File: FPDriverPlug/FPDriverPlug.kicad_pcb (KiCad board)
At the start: 2 copper layers, 21 x 61.6 mm, 4 parts, among them CN1 Conn_02x05_Odd_Even, CN2 Conn_02x16_Counter_Clockwise, U1 FP2800A

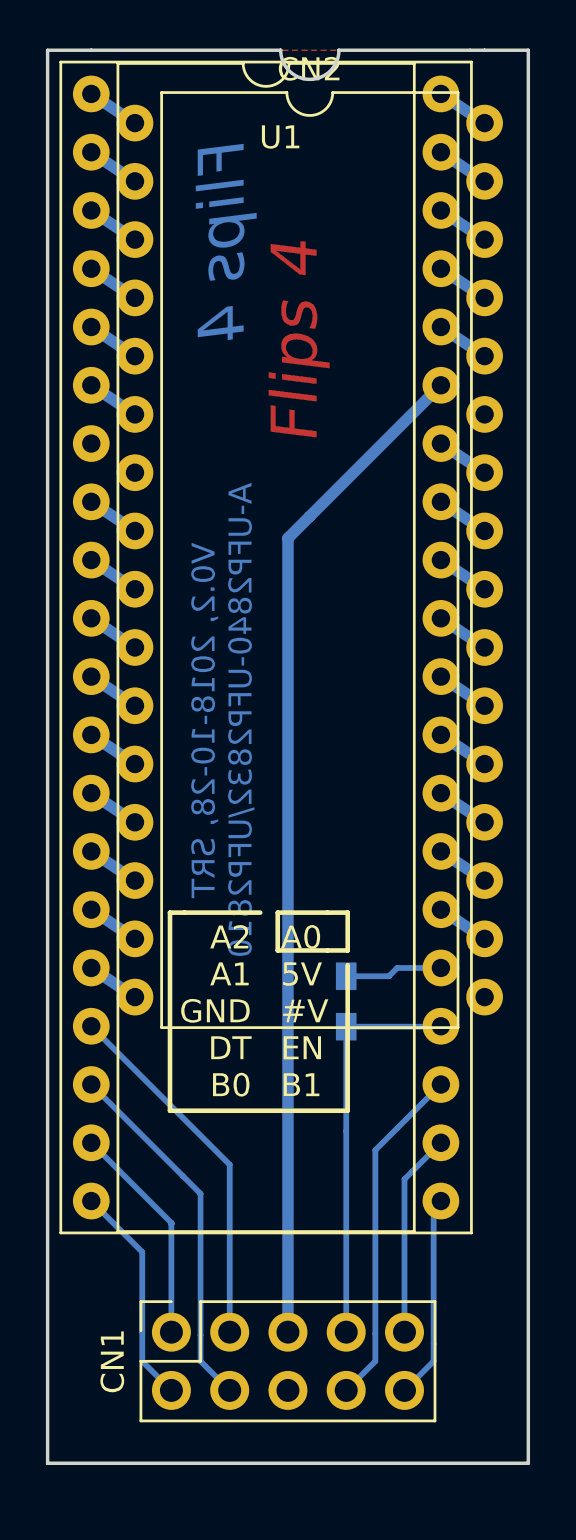
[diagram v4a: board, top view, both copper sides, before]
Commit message: Using angled IDC connector
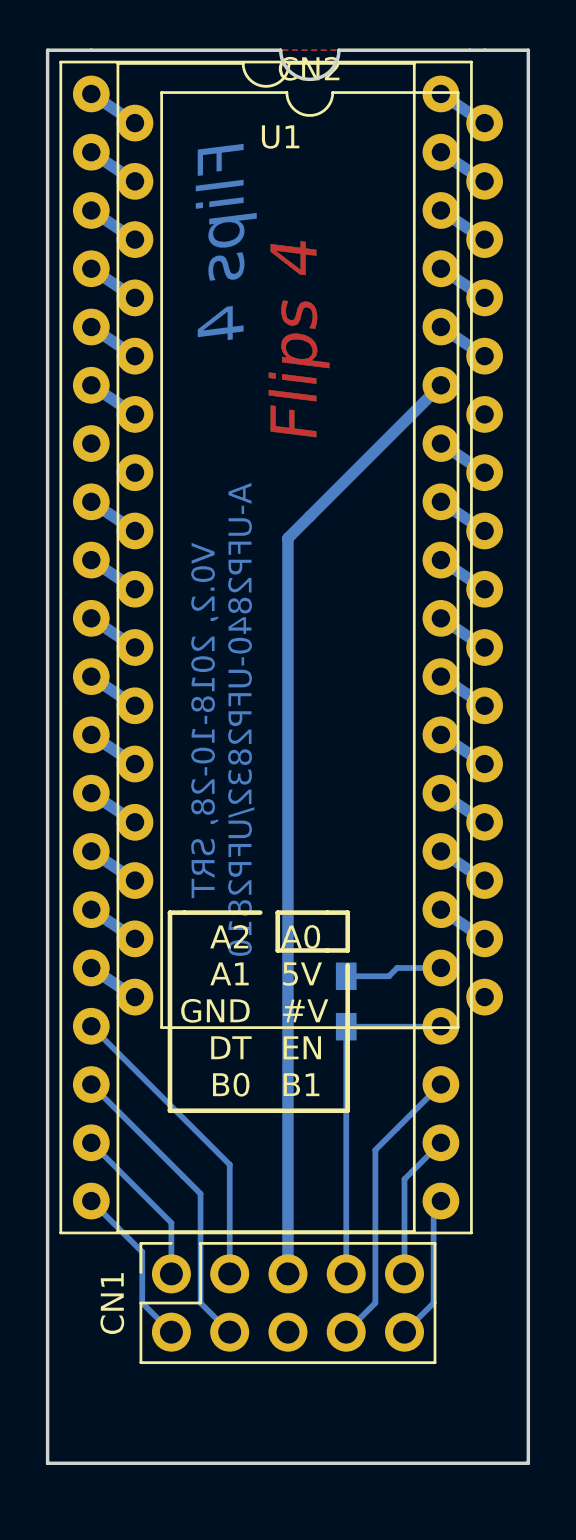
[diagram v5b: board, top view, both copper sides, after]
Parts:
- moved CN1 2.54 mm to (223.8, 118.1)
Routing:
- net /A0: track 9.83 -> 7.16 mm
- net /B1: track 8.91 -> 6.37 mm
- net VCC: track 15.8 -> 13.3 mm
- net /Enable: track 17.5 -> 14.9 mm
- net +12V: track 44.0 -> 41.5 mm
- net /Data: track 15.0 -> 12.5 mm
- net /A2: track 9.70 -> 7.16 mm
- net /A1: track 15.8 -> 13.3 mm
- net /B0: track 8.91 -> 6.82 mm
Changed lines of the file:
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@@
     (thickness 1.6)
     (drawings 29)
-    (tracks 66)
+    (tracks 60)
     (zones 0)
     (modules 4)
@@
   )
   (module Socket_Strips:Socket_Strip_Straight_2x05_Pitch2.54mm (layer F.Cu)
-    (at 223.8375 120.65 90)
+    (at 223.8375 118.11 90)
     (descr "Through hole straight socket strip, 2x05, 2.54mm pitch, double rows")
     (tags "Through hole socket strip THT 2x05 2.54mm double row")
@@
     (pad 1 thru_hole circle (at 0 0 90) (size 1.7 1.7) (drill 1) (layers *.Cu *.Mask)
       (net 39 /A0))
-    (model ${KISYS3DMOD}/Connector_IDC.3dshapes/IDC-Header_2x05_P2.54mm_Vertical.wrl
-      (offset (xyz -2.54 0 0))
+    (model ${KISYS3DMOD}/Connector_IDC.3dshapes/IDC-Header_2x05_P2.54mm_Horizontal.step
+      (offset (xyz 0 -10.15999984741211 0))
       (scale (xyz 1 1 1))
-      (rotate (xyz 0 0 0))
+      (rotate (xyz 0 0 180))
     )
   )
@@
     )
   )
+  (gr_line (start 218.44 64.77) (end 218.44 126.365) (angle 90) (layer Edge.Cuts) (width 0.15))
+  (gr_line (start 239.395 126.365) (end 239.395 64.77) (angle 90) (layer Edge.Cuts) (width 0.15))
   (dimension 61.595 (width 0.3) (layer Dwgs.User)
     (gr_text "2,4250 in" (at 251.655 95.5675 90) (layer Dwgs.User)
@@
     (arrow2b (pts (xy 200.025 126.365) (xy 199.438579 125.238496)))
   )
-  (gr_line (start 218.44 64.77) (end 218.44 126.365) (angle 90) (layer Edge.Cuts) (width 0.15))
-  (gr_line (start 239.395 126.365) (end 239.395 64.77) (angle 90) (layer Edge.Cuts) (width 0.15))
   (gr_line (start 218.44 126.365) (end 239.395 126.365) (angle 90) (layer Edge.Cuts) (width 0.15))
   (gr_line (start 239.395 64.77) (end 237.49 64.77) (angle 90) (layer Edge.Cuts) (width 0.15))
@@
   (segment (start 233.3195 105.1355) (end 233.68 104.775) (width 0.25) (layer B.Cu) (net 30))
   (segment (start 233.68 104.775) (end 235.585 104.775) (width 0.25) (layer B.Cu) (net 30) (status 800000))
-  (segment (start 226.3775 113.3475) (end 220.345 107.315) (width 0.25) (layer B.Cu) (net 31) (status 800000))
-  (segment (start 226.3775 120.65) (end 226.3775 113.3475) (width 0.25) (layer B.Cu) (net 31))
-  (segment (start 229.87 85.09) (end 235.585 79.375) (width 0.5) (layer B.Cu) (net 32))
-  (segment (start 228.9175 120.65) (end 228.9175 86.0425) (width 0.5) (layer B.Cu) (net 32))
+  (segment (start 220.345 107.315) (end 226.3775 113.3475) (width 0.25) (layer B.Cu) (net 31) (status 400000))
+  (segment (start 226.3775 113.3475) (end 226.3775 118.11) (width 0.25) (layer B.Cu) (net 31) (status 800000))
+  (segment (start 235.585 79.375) (end 229.87 85.09) (width 0.5) (layer B.Cu) (net 32))
+  (segment (start 228.9175 86.0425) (end 228.9175 118.11) (width 0.5) (layer B.Cu) (net 32) (status 800000))
   (segment (start 228.9175 86.0425) (end 229.87 85.09) (width 0.5) (layer B.Cu) (net 32))
   (segment (start 235.2675 115.2525) (end 235.585 114.935) (width 0.25) (layer B.Cu) (net 33) (status C00000))
-  (segment (start 235.2675 121.92) (end 233.9975 123.19) (width 0.25) (layer B.Cu) (net 33))
-  (segment (start 235.2675 121.158) (end 235.2675 121.92) (width 0.25) (layer B.Cu) (net 33))
-  (segment (start 235.2675 121.158) (end 235.2675 115.2525) (width 0.25) (layer B.Cu) (net 33))
+  (segment (start 233.9975 120.65) (end 235.2675 119.38) (width 0.25) (layer B.Cu) (net 33) (status 400000))
+  (segment (start 235.2675 119.38) (end 235.2675 115.2525) (width 0.25) (layer B.Cu) (net 33) (status 800000))
+  (segment (start 235.2675 115.2525) (end 235.585 114.935) (width 0.25) (layer B.Cu) (net 33) (status C00000))
   (segment (start 235.585 112.395) (end 234.315 113.665) (width 0.25) (layer B.Cu) (net 34))
+  (segment (start 233.9975 113.9825) (end 233.9975 118.11) (width 0.25) (layer B.Cu) (net 34) (status 800000))
   (segment (start 233.9975 113.9825) (end 234.315 113.665) (width 0.25) (layer B.Cu) (net 34))
-  (segment (start 233.9975 120.65) (end 233.9975 113.9825) (width 0.25) (layer B.Cu) (net 34))
   (segment (start 235.585 109.855) (end 233.68 111.76) (width 0.25) (layer B.Cu) (net 35) (status 400000))
+  (segment (start 232.7275 119.38) (end 232.7275 112.7125) (width 0.25) (layer B.Cu) (net 35))
+  (segment (start 232.7275 119.38) (end 231.4575 120.65) (width 0.25) (layer B.Cu) (net 35) (status 800000))
   (segment (start 232.7275 112.7125) (end 233.68 111.76) (width 0.25) (layer B.Cu) (net 35))
-  (segment (start 232.7275 121.92) (end 231.4575 123.19) (width 0.25) (layer B.Cu) (net 35))
-  (segment (start 232.7275 120.7135) (end 232.7275 121.92) (width 0.25) (layer B.Cu) (net 35))
-  (segment (start 232.7275 120.7135) (end 232.7275 112.7125) (width 0.25) (layer B.Cu) (net 35))
-  (segment (start 231.4575 111.887) (end 231.4575 120.65) (width 0.25) (layer B.Cu) (net 36))
   (segment (start 231.4575 107.3355) (end 235.5645 107.3355) (width 0.25) (layer B.Cu) (net 36) (status C00000))
   (segment (start 235.5645 107.3355) (end 235.585 107.315) (width 0.25) (layer B.Cu) (net 36) (status C00000))
-  (segment (start 231.4575 111.887) (end 231.4575 107.3355) (width 0.25) (layer B.Cu) (net 36) (status 800000))
+  (segment (start 231.4575 118.11) (end 231.4575 107.3355) (width 0.25) (layer B.Cu) (net 36) (status C00000))
   (segment (start 220.345 109.855) (end 224.3455 113.8555) (width 0.25) (layer B.Cu) (net 37) (status 400000))
+  (segment (start 225.1075 119.38) (end 225.1075 114.6175) (width 0.25) (layer B.Cu) (net 37))
+  (segment (start 225.1075 119.38) (end 226.3775 120.65) (width 0.25) (layer B.Cu) (net 37) (status 800000))
   (segment (start 225.1075 114.6175) (end 224.3455 113.8555) (width 0.25) (layer B.Cu) (net 37))
-  (segment (start 225.1075 121.92) (end 226.3775 123.19) (width 0.25) (layer B.Cu) (net 37))
-  (segment (start 225.1075 120.777) (end 225.1075 121.92) (width 0.25) (layer B.Cu) (net 37))
-  (segment (start 225.1075 120.777) (end 225.1075 114.6175) (width 0.25) (layer B.Cu) (net 37))
-  (segment (start 222.5675 117.1575) (end 220.345 114.935) (width 0.25) (layer B.Cu) (net 38) (status 800000))
-  (segment (start 222.5675 121.92) (end 223.8375 123.19) (width 0.25) (layer B.Cu) (net 38))
-  (segment (start 222.5675 120.65) (end 222.5675 121.92) (width 0.25) (layer B.Cu) (net 38))
-  (segment (start 222.5675 120.65) (end 222.5675 117.1575) (width 0.25) (layer B.Cu) (net 38))
-  (segment (start 223.8375 115.8875) (end 220.345 112.395) (width 0.25) (layer B.Cu) (net 39) (status 800000))
-  (segment (start 223.8375 115.8875) (end 223.8375 115.951) (width 0.25) (layer B.Cu) (net 39))
-  (segment (start 223.8375 115.951) (end 223.8375 115.8875) (width 0.25) (layer B.Cu) (net 39))
-  (segment (start 223.8375 120.65) (end 223.8375 115.8875) (width 0.25) (layer B.Cu) (net 39))
+  (segment (start 220.345 114.935) (end 222.5675 117.1575) (width 0.25) (layer B.Cu) (net 38) (status 400000))
+  (segment (start 222.5675 119.38) (end 222.5675 117.1575) (width 0.25) (layer B.Cu) (net 38))
+  (segment (start 222.5675 119.38) (end 223.8375 120.65) (width 0.25) (layer B.Cu) (net 38) (status 800000))
+  (segment (start 220.345 112.395) (end 223.8375 115.8875) (width 0.25) (layer B.Cu) (net 39) (status 400000))
+  (segment (start 223.8375 115.8875) (end 223.8375 118.11) (width 0.25) (layer B.Cu) (net 39) (status 800000))
   (zone (net 30) (net_name GND) (layer F.Cu) (hatch edge 0.508)
     (connect_pads (clearance 0.1524))

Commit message: Rework silkscreen
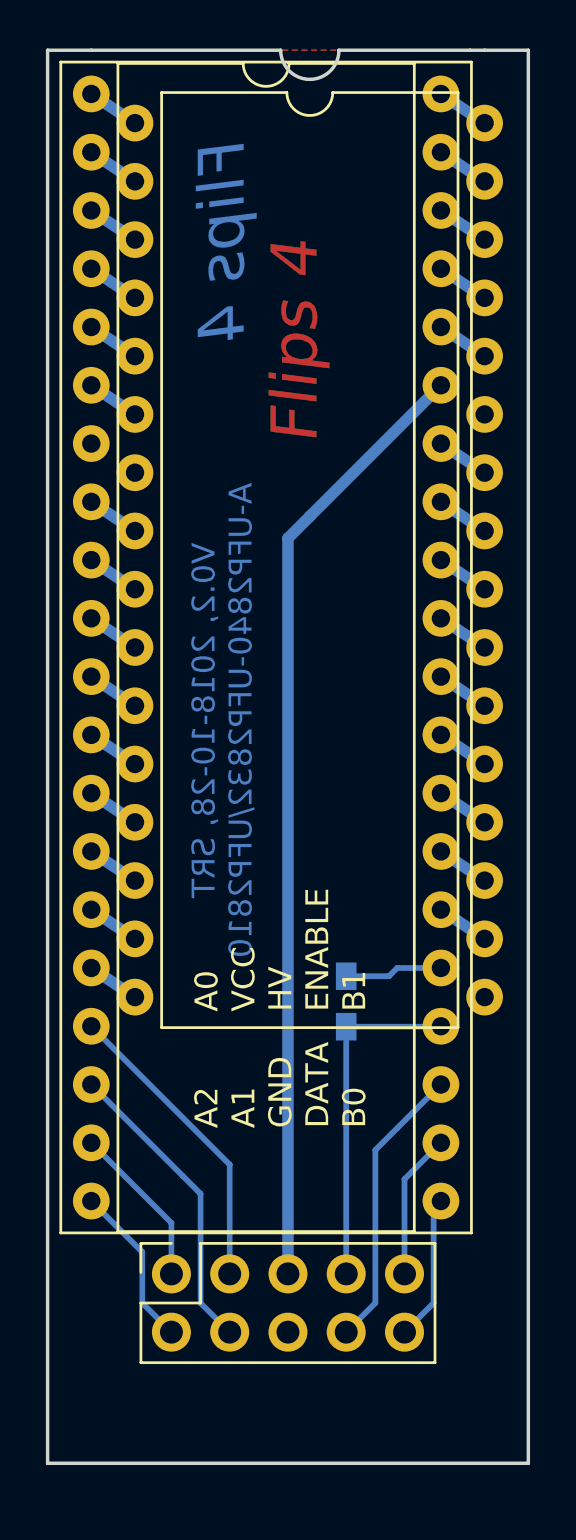
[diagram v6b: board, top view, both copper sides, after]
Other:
- board text added: "A0 VCC HV ENABLE B1"
- board text added: "A2 A1 GND DATA B0"
- board text removed: "A0 5V #V EN B1"
- board text removed: "A2 A1 GND DT B0"
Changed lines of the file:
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@@
   (general
     (thickness 1.6)
-    (drawings 29)
+    (drawings 18)
     (tracks 60)
     (zones 0)
@@
     (descr "Through hole straight socket strip, 2x05, 2.54mm pitch, double rows")
     (tags "Through hole socket strip THT 2x05 2.54mm double row")
-    (fp_text reference CN1 (at -1.27 -2.54 90) (layer F.SilkS)
+    (fp_text reference CN1 (at -1.27 -2.54 90) (layer F.SilkS) hide
       (effects (font (size 1 1) (thickness 0.15)))
     )
@@
     (descr "40-lead though-hole mounted DIP package, row spacing 15.24 mm (600 mils), Socket")
     (tags "THT DIP DIL PDIP 2.54mm 15.24mm 600mil Socket")
-    (fp_text reference U1 (at 8.255 1.905) (layer F.SilkS)
+    (fp_text reference U1 (at 8.255 1.905) (layer F.SilkS) hide
       (effects (font (size 1 1) (thickness 0.15)))
     )
@@
     (descr "32-lead though-hole mounted DIP package, row spacing 15.24 mm (600 mils)")
     (tags "THT DIP DIL PDIP 2.54mm 15.24mm 600mil")
-    (fp_text reference CN2 (at 7.62 -2.33) (layer F.SilkS)
+    (fp_text reference CN2 (at 7.62 -2.33) (layer F.SilkS) hide
       (effects (font (size 1 1) (thickness 0.15)))
     )
@@
     (effects (font (size 2 2) (thickness 0.5) italic) (justify mirror))
   )
-  (gr_text "A0\n5V\n#V\nEN\nB1" (at 228.6 106.68) (layer F.SilkS)
+  (gr_text "A0\nVCC\nHV\nENABLE\nB1" (at 228.6 106.68 90) (layer F.SilkS)
     (effects (font (size 1 1) (thickness 0.2)) (justify left))
   )
-  (gr_line (start 230.632 104.013) (end 231.521 104.013) (angle 90) (layer F.SilkS) (width 0.2))
-  (gr_line (start 231.521 102.362) (end 230.632 102.362) (angle 90) (layer F.SilkS) (width 0.2))
-  (gr_line (start 231.521 104.013) (end 231.521 102.362) (angle 90) (layer F.SilkS) (width 0.2))
-  (gr_line (start 231.521 110.998) (end 231.521 104.648) (angle 90) (layer F.SilkS) (width 0.2))
-  (gr_line (start 223.774 110.998) (end 231.521 110.998) (angle 90) (layer F.SilkS) (width 0.2))
-  (gr_line (start 223.774 102.362) (end 223.774 110.998) (angle 90) (layer F.SilkS) (width 0.2))
-  (gr_line (start 224.409 102.362) (end 223.774 102.362) (angle 90) (layer F.SilkS) (width 0.2))
-  (gr_line (start 227.711 102.362) (end 224.409 102.362) (angle 90) (layer F.SilkS) (width 0.2))
-  (gr_line (start 230.632 104.013) (end 228.473 104.013) (angle 90) (layer F.SilkS) (width 0.2))
-  (gr_line (start 228.473 102.362) (end 230.632 102.362) (angle 90) (layer F.SilkS) (width 0.2))
-  (gr_line (start 228.473 104.013) (end 228.473 102.362) (angle 90) (layer F.SilkS) (width 0.2))
-  (gr_text "A2\nA1\nGND\nDT\nB0" (at 227.33 106.68) (layer F.SilkS)
-    (effects (font (size 1 1) (thickness 0.2)) (justify right))
+  (gr_text "A2\nA1\nGND\nDATA\nB0" (at 228.6 111.76 90) (layer F.SilkS)
+    (effects (font (size 1 1) (thickness 0.2)) (justify left))
   )
   (dimension 20.955 (width 0.3) (layer Dwgs.User)

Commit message: adding Flips4 label to front
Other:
- board text added: "Flips4"
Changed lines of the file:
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@@
   (general
     (thickness 1.6)
-    (drawings 18)
+    (drawings 19)
     (tracks 60)
     (zones 0)
@@
     )
   )
+  (gr_text Flips4 (at 238.125 108.077 90) (layer F.Cu)
+    (effects (font (size 1.2 1.2) (thickness 0.24) italic) (justify right))
+  )
   (gr_line (start 218.44 64.77) (end 218.44 126.365) (angle 90) (layer Edge.Cuts) (width 0.15))
